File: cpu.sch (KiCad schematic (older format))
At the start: 28 parts, among them SW1 RESET, SW2 STEP, U1 Z80CPU, U2 74HC04, Y1 7.3728MHz

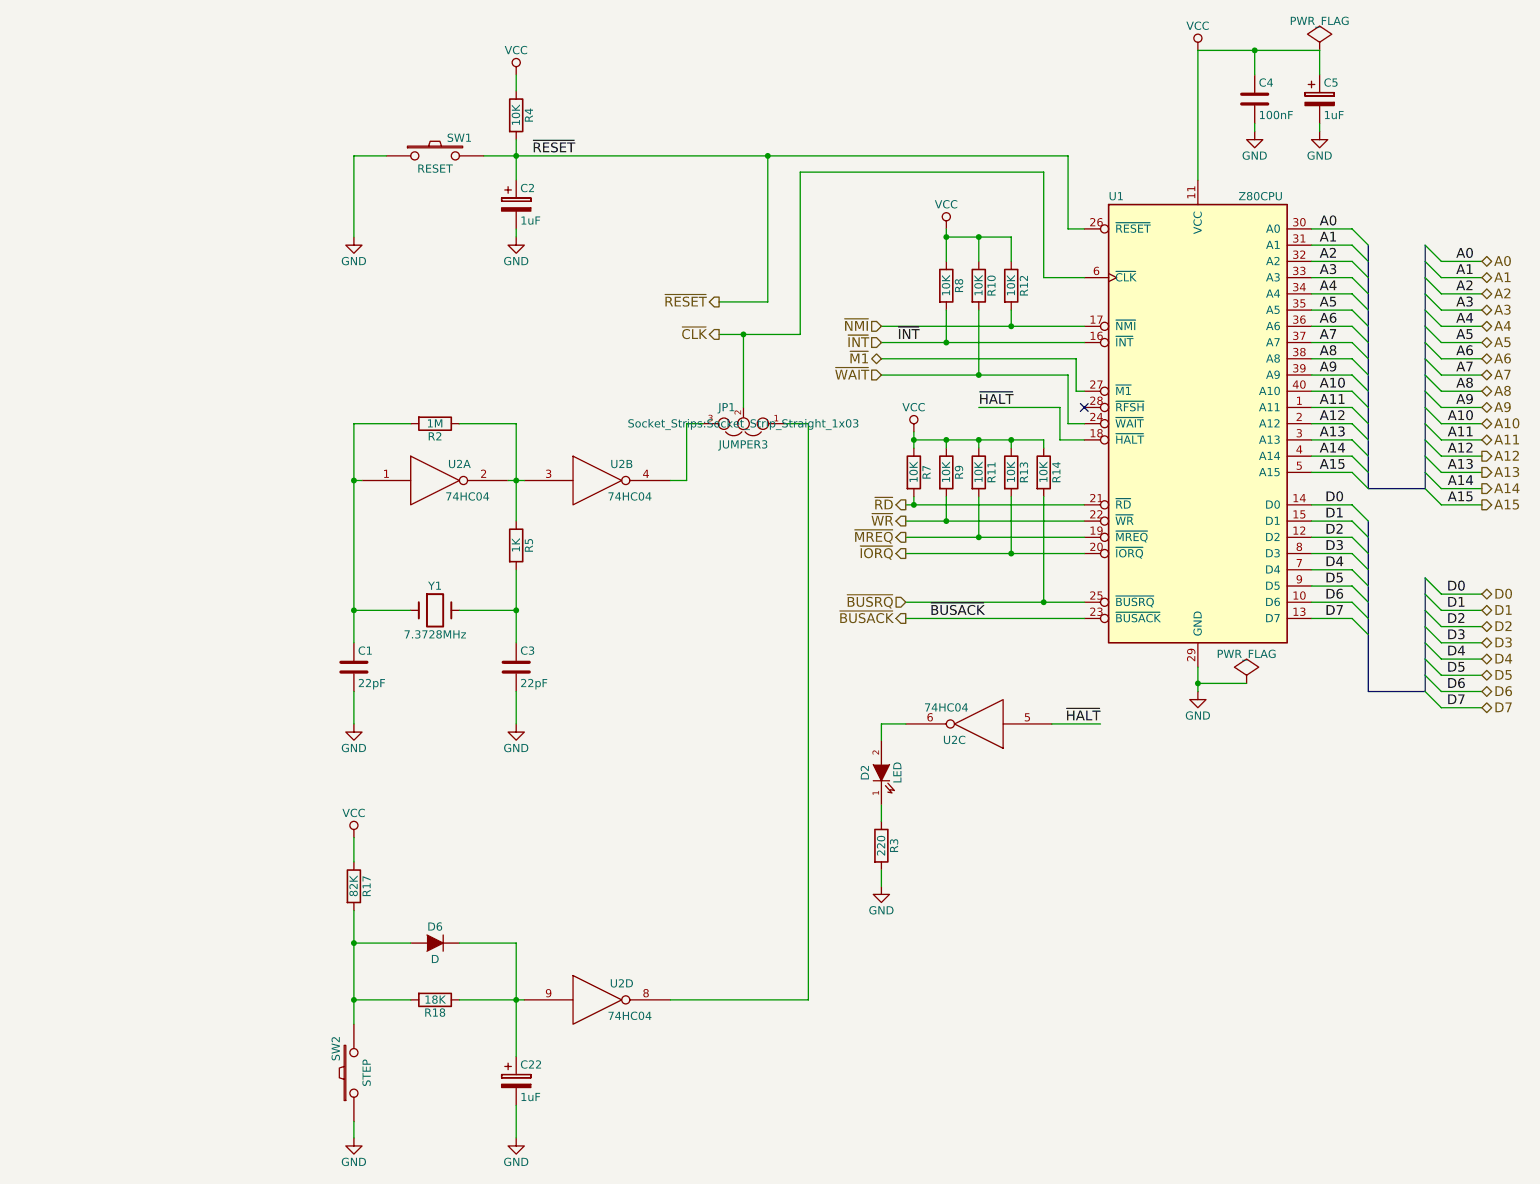
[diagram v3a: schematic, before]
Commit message: Update PCB, better layout. Got Addr bus back in order
Think having both USB and DC input would be useful. Switchmode a plus
then plugpack/battery etc voltage doesn't matter. Plus I have a bag full
of those parts too!

I've refdes'd the linear reg just to deal with the net. Will remove if
we both are happy with switcher. Linear cheaper to kit out I guess.

Was trying to find a better way to combine USB and DC power rails than
just schottky diodes. If you have any ideas.

Going to have a big area under the IO ports, might be worth adding a USB
to serial, or sacrifice a IO port for some blinky LEDs and buttons?
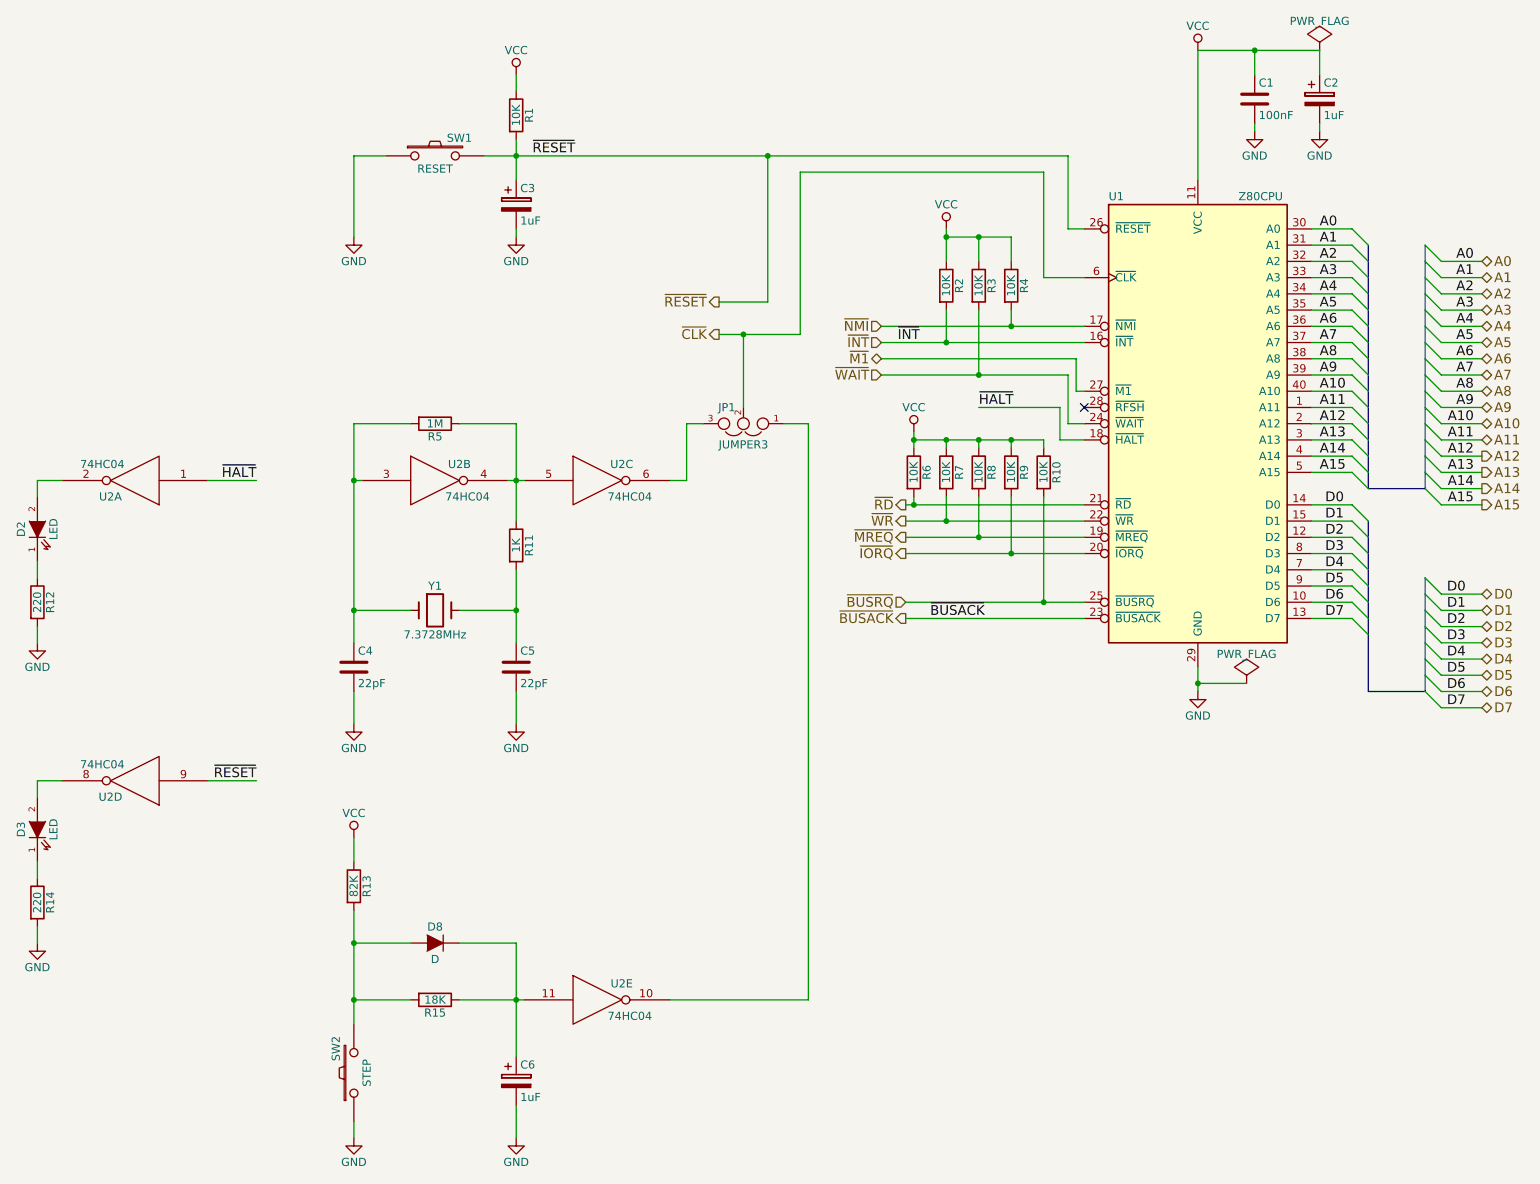
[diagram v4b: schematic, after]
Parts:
- added D3: LED, LEDs:LED_1206, symbol LED
- added R14: 220, Resistors_SMD:R_0805_HandSoldering, symbol R
- added unit 4 of U2
- D2: footprint LEDs:LED-3MM -> LEDs:LED_1206
- JP1: footprint Socket_Strips:Socket_Strip_Straight_1x03 -> Pin_Headers:Pin_Header_Straight_1x03
- U1: footprint Housings_DIP:DIP-40_W25.4mm_LongPads -> Housings_DIP:DIP-40_W15.24mm_LongPads
- renumbered C4 to C1, C5 to C2, C2 to C3, C1 to C4, C3 to C5, C22 to C6, D6 to D8, R4 to R1, R14 to R10, R5 to R11, R3 to R12, R17 to R13, R18 to R15, R8 to R2, R10 to R3, R12 to R4, R2 to R5, R7 to R6, R9 to R7, R11 to R8, R13 to R9
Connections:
- net GND: now also R14.2, U2.7 (GND)
- net VCC: now also U2.14 (VCC)
- net ~HALT: now also U2.1; no longer U2.5
- net ~RESET: now also U2.9
- net at R11.1, R5.1: now also U2.4, U2.5; no longer U2.2, U2.3
- net at JP1.3: now also U2.6; no longer U2.4
- net at C4.1, R5.2, Y1.1: now also U2.3; no longer U2.1
- net at D2.2 (A): now also U2.2; no longer U2.6
- net at JP1.1: now also U2.10; no longer U2.8
- net at C6.1, D8.1 (K), R15.1: now also U2.11; no longer U2.9
- new net: D3.2 (A), U2.8
- new net: D3.1 (K), R14.1
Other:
- moved on the sheet: D2, R12

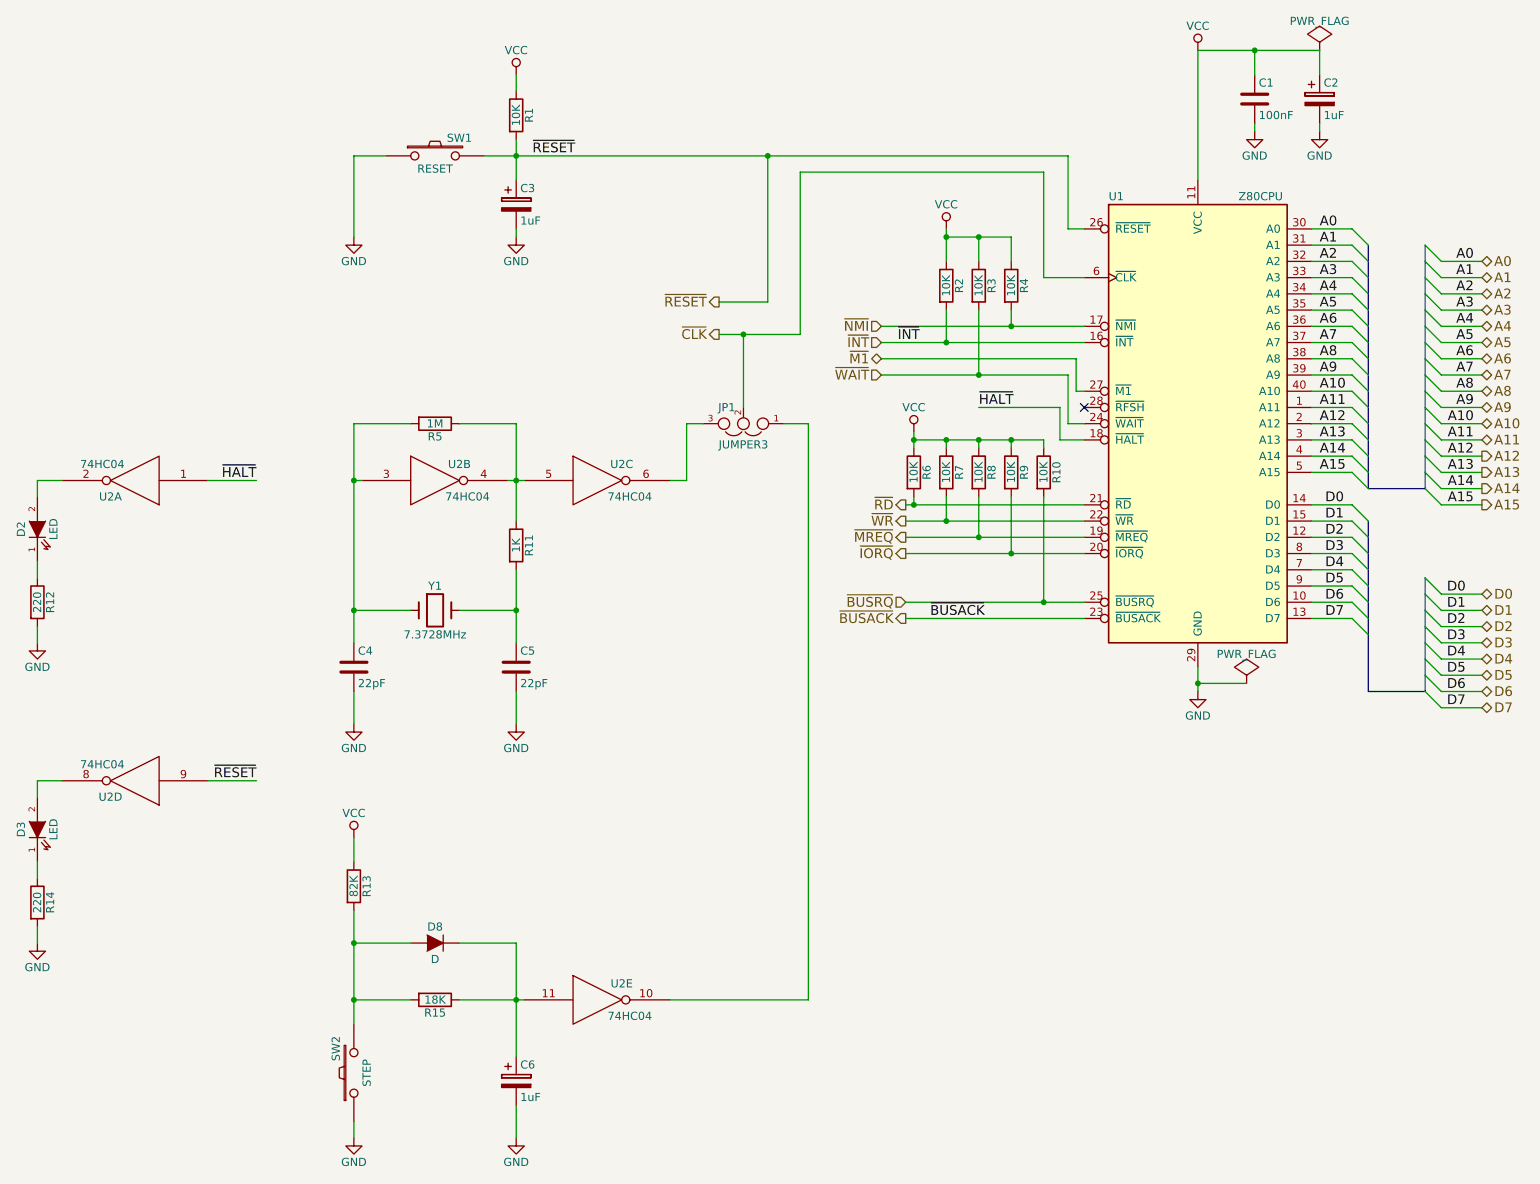
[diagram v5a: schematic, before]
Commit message: Update with smaller board and through-hole parts.
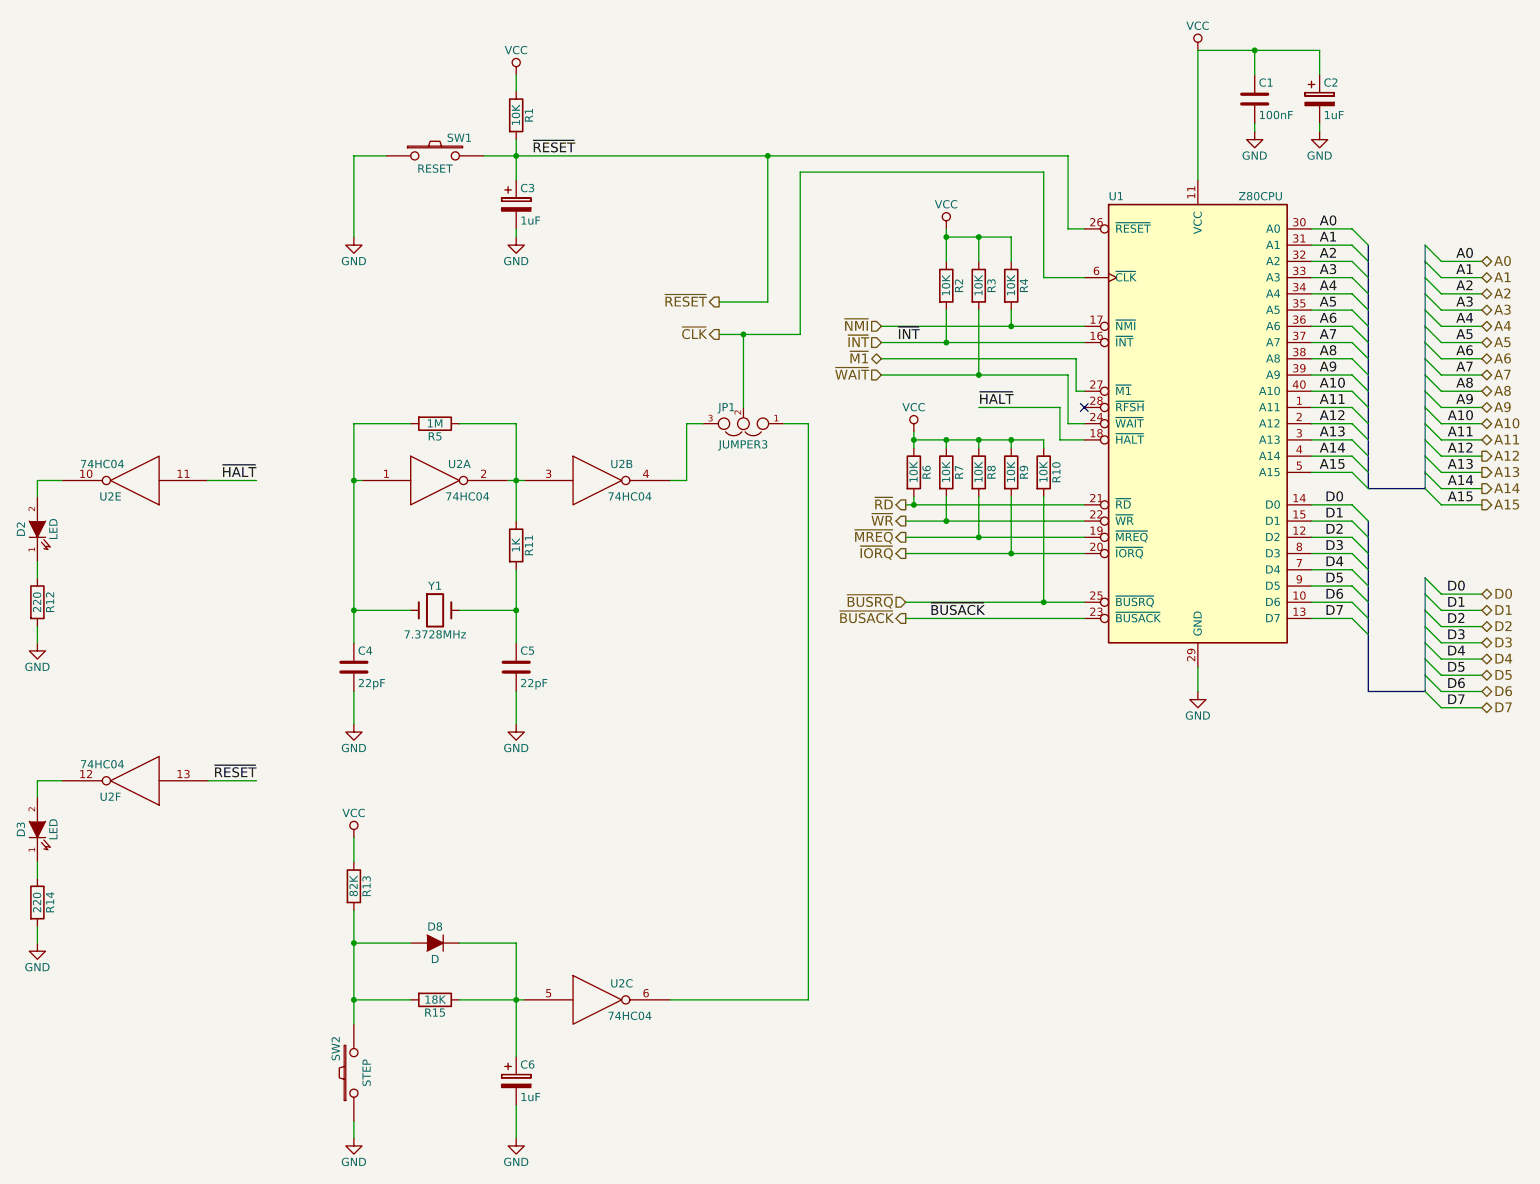
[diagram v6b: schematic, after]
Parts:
- C1: footprint Capacitors_SMD:C_0805_HandSoldering -> Capacitors_ThroughHole:C_Rect_L4_W2.5_P2.5
- C2, C3: footprint Capacitors_SMD:c_elec_4x4.5 -> Capacitors_ThroughHole:C_Radial_D5_L6_P2.5
- C4, C5: footprint Capacitors_SMD:C_0805_HandSoldering -> Capacitors_ThroughHole:C_Disc_D3_P2.5
- C6: footprint Capacitors_SMD:c_elec_4x4.5 -> Capacitors_ThroughHole:C_Radial_D5_L11_P2.5
- D2, D3: footprint LEDs:LED_1206 -> LEDs:LED-3MM
- D8: footprint Diodes_SMD:MiniMELF_Standard -> Diodes_ThroughHole:Diode_DO-41_SOD81_Horizontal_RM10
- R1, R10, R11, R12, R13, R14, R15, R2, R3, R4, R5, R6, R7, R8, R9: footprint Resistors_SMD:R_0805_HandSoldering -> Resistors_ThroughHole:Resistor_Horizontal_RM7mm
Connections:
- net ~HALT: now also U2.11; no longer U2.1
- net ~RESET: now also U2.13; no longer U2.9
- net at R11.1, R5.1: now also U2.2, U2.3; no longer U2.4, U2.5
- net at JP1.3: now also U2.4; no longer U2.6
- net at C4.1, R5.2, Y1.1: now also U2.1; no longer U2.3
- net at D2.2 (A): now also U2.10; no longer U2.2
- net at JP1.1: now also U2.6; no longer U2.10
- net at C6.1, D8.1 (K), R15.1: now also U2.5; no longer U2.11
- net at D3.2 (A): now also U2.12; no longer U2.8

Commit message: Smaller, through hole, done!
Apart from maybe a few footprint issues and a bit of trace fiddling this
should be pretty close. Be interesting how much this will cost now. :)
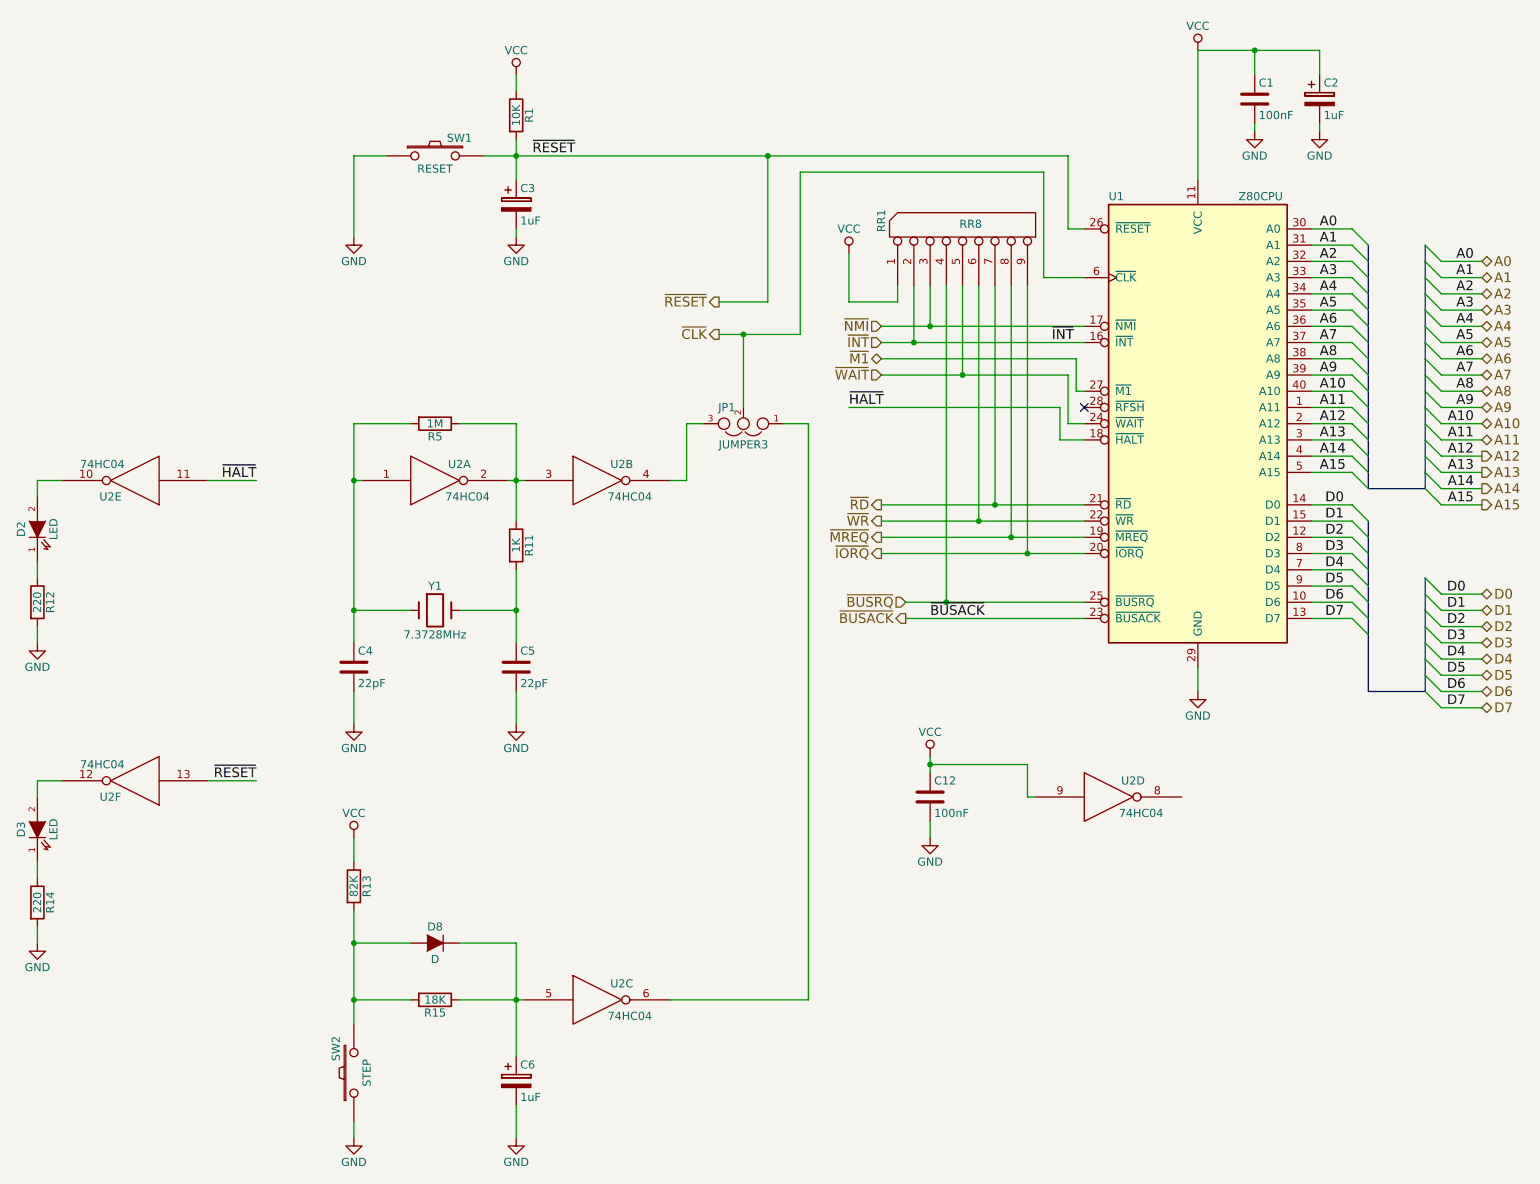
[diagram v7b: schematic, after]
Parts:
- removed R10, R2, R3, R4, R6, R7, R8, R9: 10K, Resistors_ThroughHole:Resistor_Horizontal_RM7mm, symbol R
- added C12: 100nF, Capacitors_ThroughHole:C_Rect_L4_W2.5_P2.5, symbol C
- added RR1: RR8, Resistors_ThroughHole:Resistor_Array_SIP8, symbol RR8
- added unit 4 of U2
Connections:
- net GND: now also C12.2, U2.7 (GND)
- net VCC: now also C12.1, RR1.1 (COM), U2.14 (VCC), U2.9
- net ~BUSRQ: now also RR1.4
- net ~INT: now also RR1.2
- net ~IORQ: now also RR1.9
- net ~MREQ: now also RR1.8
- net ~NMI: now also RR1.3
- net ~RD: now also RR1.7
- net ~WAIT: now also RR1.5
- net ~WR: now also RR1.6
